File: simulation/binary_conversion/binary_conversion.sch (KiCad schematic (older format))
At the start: 84 parts, among them J1 Conn_01x06_Male, J2 Conn_01x06_Male, M1 2N7002, M10 2N7002, M11 2N7002, M12 2N7002, M13 2N7002, M14 2N7002, M15 2N7002, M16 2N7002, M17 BSS84, M18 2N7002, M19 2N7002, M2 2N7002, M20 2N7002, M21 2N7002, M22 2N7002, M23 2N7002, M24 2N7002, M25 2N7002, M26 2N7002, M27 2N7002, M28 2N7002, M29 2N7002, M3 2N7002, M30 2N7002, M31 2N7002, M32 2N7002, M33 2N7002, M34 BSS84, M35 2N7002, M36 2N7002, M37 2N7002, M38 2N7002, M39 2N7002, M4 2N7002, M40 2N7002, M41 2N7002, M42 2N7002, M43 2N7002, M44 2N7002, M45 2N7002, M46 2N7002, M47 2N7002, M48 2N7002, M49 2N7002, M5 2N7002, M50 BSS84, M51 2N7002, M52 2N7002, M53 2N7002, M54 2N7002, M55 2N7002, M56 2N7002, M57 2N7002, M58 2N7002, M59 2N7002, M6 2N7002, M60 2N7002, M61 2N7002, M62 2N7002, M63 2N7002, M64 2N7002, M65 BSS84, M66 2N7002, M67 2N7002, M68 2N7002, M69 2N7002, M7 2N7002, M70 2N7002, M71 2N7002, M72 2N7002, M73 2N7002, M74 2N7002, M75 2N7002, M76 2N7002, M77 2N7002, M78 2N7002, M79 2N7002, M8 2N7002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

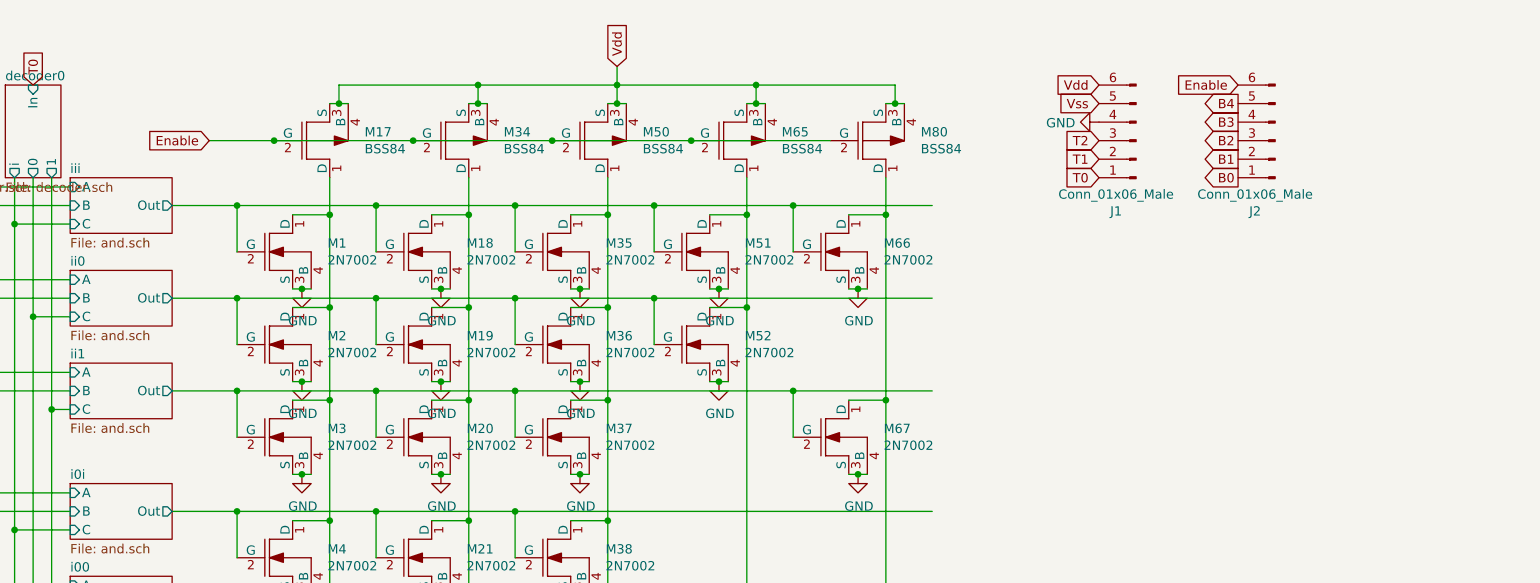
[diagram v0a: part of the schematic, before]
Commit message: ternary adders, switches, and cyclers
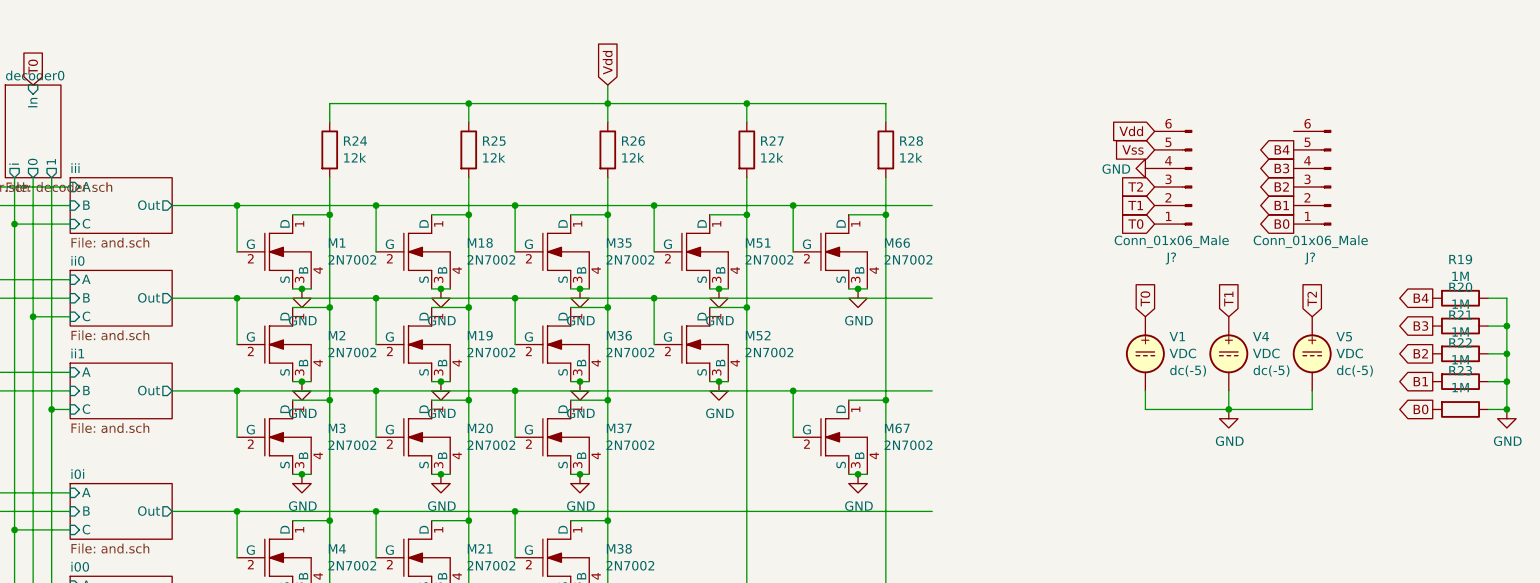
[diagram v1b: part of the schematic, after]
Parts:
- removed J1, J2: Conn_01x06_Male, symbol Connector:Conn_01x06_Male
- removed M17, M34, M50, M65, M80: BSS84, symbol pspice:MPMOS
- added J? (x2): Conn_01x06_Male, symbol Connector:Conn_01x06_Male
- added R19, R20, R21, R22, R23: 1M, symbol Device:R
- added R24, R25, R26, R27, R28: 12k, symbol Device:R
- added V1, V4, V5: VDC, symbol Simulation_SPICE:VDC
- M1, M10, M11, M12, M13, M14, M15, M16, M18, M19, M2, M20, M21, M22, M23, M24, M25, M26, M27, M28, M29, M3, M30, M31, M32, M33, M35, M36, M37, M38, M39, M4, M40, M41, M42, M43, M44, M45, M46, M47, M48, M49, M5, M51, M52, M53, M54, M55, M56, M57, M58, M59, M6, M60, M61, M62, M63, M64, M66, M67, M68, M69, M7, M70, M71, M72, M73, M74, M75, M76, M77, M78, M79, M8, M9: Spice_Lib_File (none) -> /lab/dev/tritium/simulation/spice/mos.lib; Spice_Model (none) -> 2N7002; Spice_Netlist_Enabled (none) -> Y; Spice_Primitive (none) -> M
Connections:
- net labels removed: Enable
- wire segments 681 -> 680

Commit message: update readme.md to include current project status
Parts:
- gave numbers to parts that had none: 2
